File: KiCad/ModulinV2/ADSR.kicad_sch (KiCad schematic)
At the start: 71 parts, among them IC48 TL074HIDR, IC49 AS3310D, IC50 AS3310D

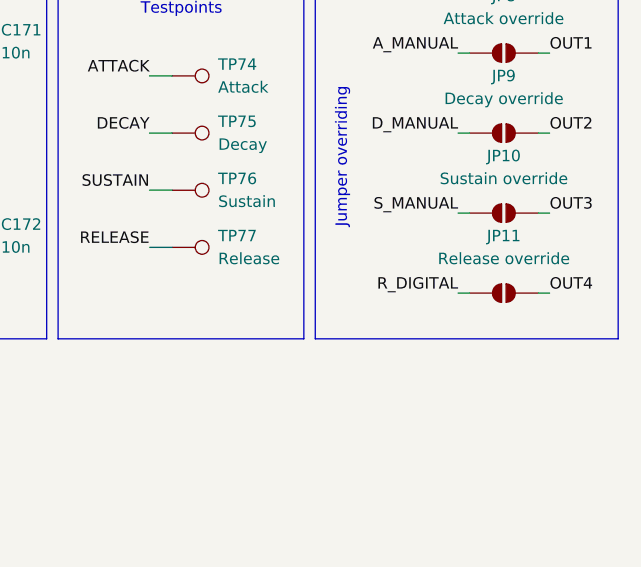
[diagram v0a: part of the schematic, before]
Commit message: Completed VCF and VCA layouts, started with ADSR
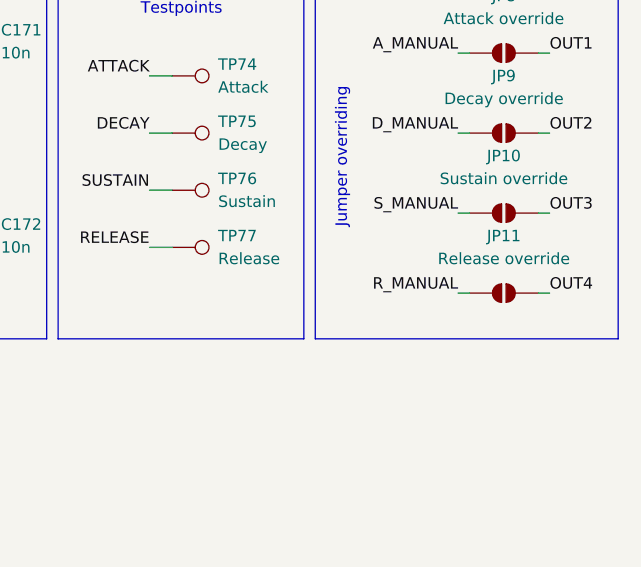
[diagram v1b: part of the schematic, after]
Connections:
- net R_DIGITAL: no longer JP11.2 (B)
- net R_MANUAL: now also JP11.2 (B)
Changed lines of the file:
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@@
 		)
 	)
-	(label "R_DIGITAL"
+	(label "R_MANUAL"
 		(at 265.43 160.02 180)
 		(effects

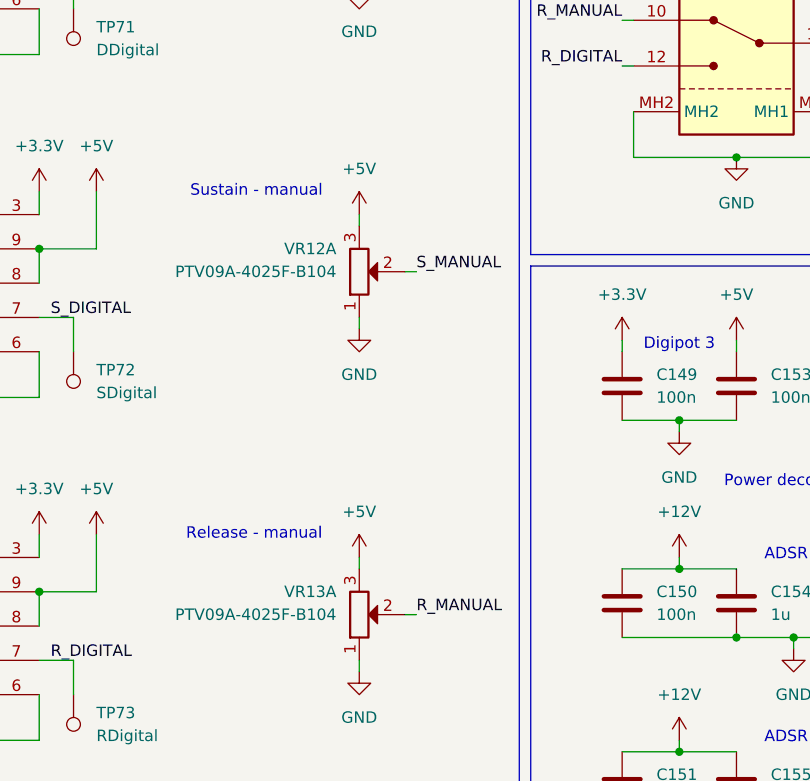
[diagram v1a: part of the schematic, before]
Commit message: Completed ADSR layout, started with Waveform select
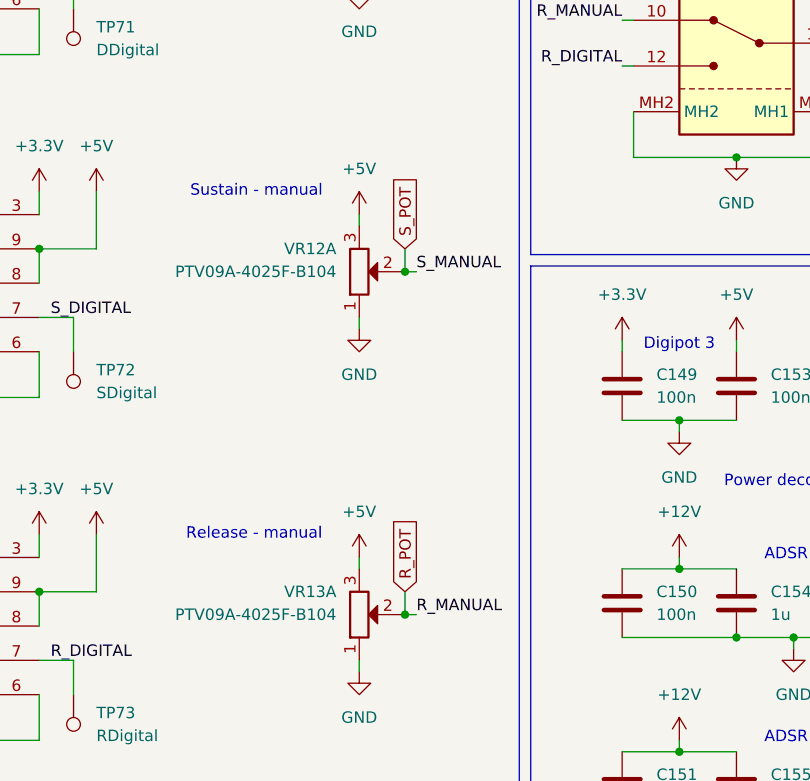
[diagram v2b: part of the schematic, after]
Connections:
- net R_MANUAL renamed R_POT
- net S_MANUAL renamed S_POT
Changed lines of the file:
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@@
 	)
 	(junction
+		(at 95.25 106.68)
+		(diameter 0)
+		(color 0 0 0 0)
+	)
+	(junction
 		(at 54.61 142.24)
 		(diameter 0)
@@
 	)
 	(junction
+		(at 95.25 144.78)
+		(diameter 0)
+		(color 0 0 0 0)
+	)
+	(junction
 		(at 171.45 87.63)
 		(diameter 0)
@@
 	(wire
 		(pts
+			(xy 95.25 142.24) (xy 95.25 144.78)
+		)
+		(stroke
+			(width 0)
+			(type default)
+		)
+	)
+	(wire
+		(pts
 			(xy 149.86 85.09) (xy 149.86 78.74)
 		)
@@
 	(wire
 		(pts
+			(xy 95.25 104.14) (xy 95.25 106.68)
+		)
+		(stroke
+			(width 0)
+			(type default)
+		)
+	)
+	(wire
+		(pts
 			(xy 171.45 55.88) (xy 166.37 55.88)
 		)
@@
 		)
 	)
+	(global_label "S_POT"
+		(shape input)
+		(at 95.25 104.14 90)
+		(fields_autoplaced yes)
+		(effects
+			(font
+				(size 1.27 1.27)
+			)
+			(justify left)
+		)
+		(property "Intersheetrefs" "${INTERSHEET_REFS}"
+			(at 95.25 95.4096 90)
+			(effects
+				(font
+					(size 1.27 1.27)
+				)
+				(justify left)
+				(hide yes)
+			)
+		)
+	)
+	(global_label "R_POT"
+		(shape input)
+		(at 95.25 142.24 90)
+		(fields_autoplaced yes)
+		(effects
+			(font
+				(size 1.27 1.27)
+			)
+			(justify left)
+		)
+		(property "Intersheetrefs" "${INTERSHEET_REFS}"
+			(at 95.25 133.4491 90)
+			(effects
+				(font
+					(size 1.27 1.27)
+				)
+				(justify left)
+				(hide yes)
+			)
+		)
+	)

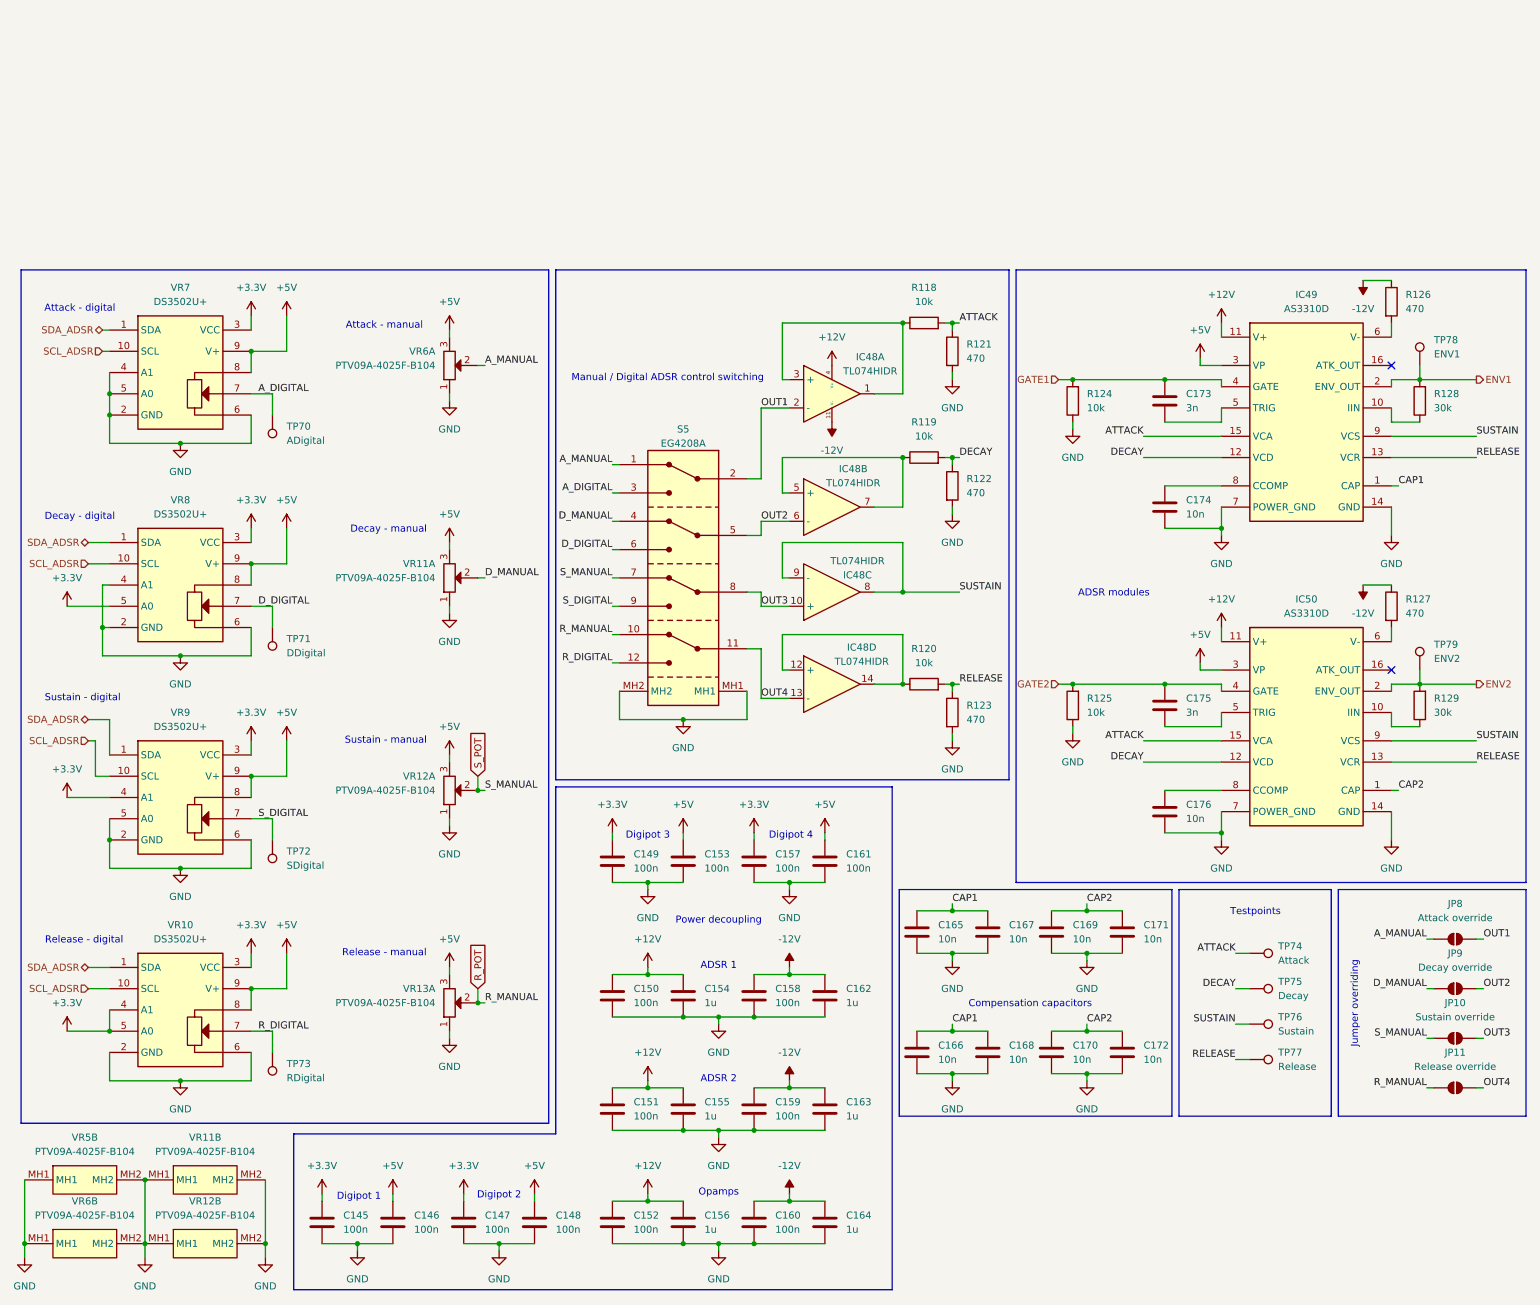
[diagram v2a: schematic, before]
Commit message: Fixed schematic connections
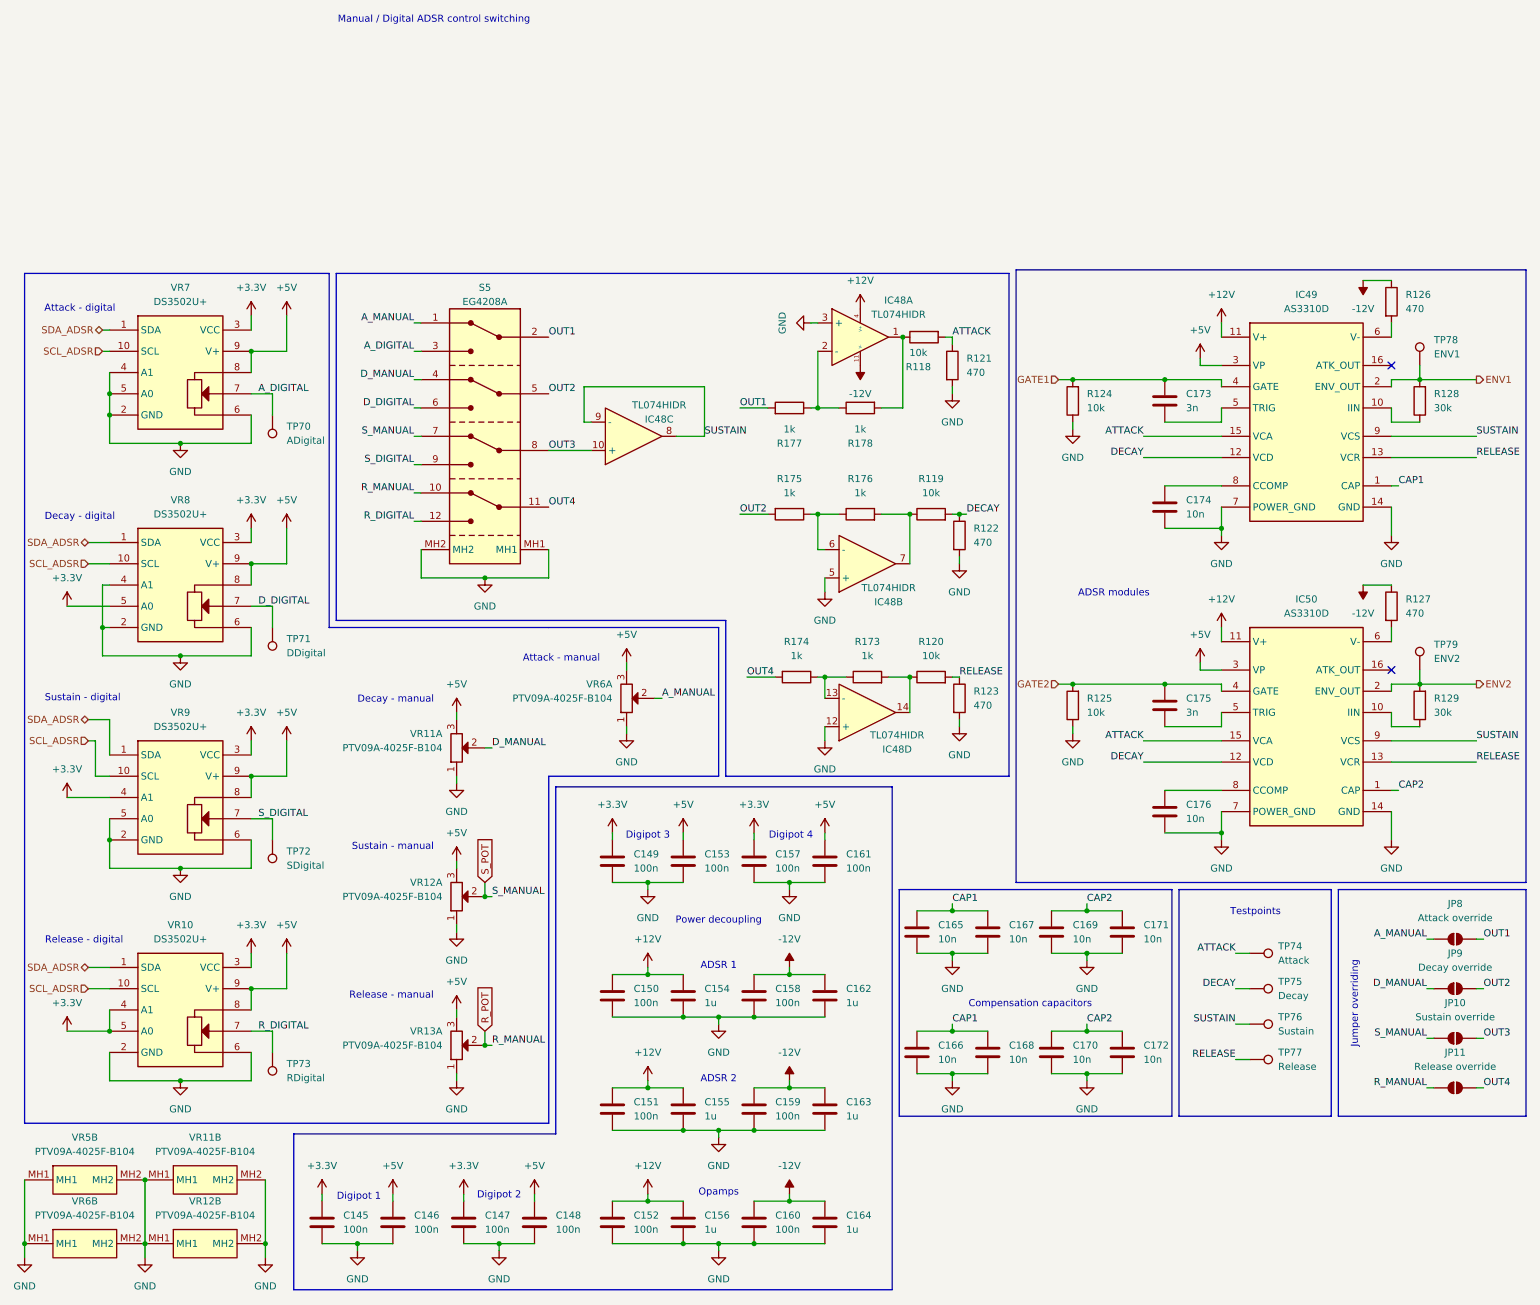
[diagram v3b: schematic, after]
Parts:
- added R173, R174, R175, R176, R177, R178: 1k, Resistor_SMD:R_0603_1608Metric_Pad0.98x0.95mm_HandSolder, symbol Device:R
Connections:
- net GND: now also IC48.12 (+), IC48.3 (+), IC48.5 (+)
- net OUT1: now also R177.2; no longer IC48.2 (-)
- net OUT2: now also R175.2; no longer IC48.6 (-)
- net OUT4: now also R174.2; no longer IC48.13 (-)
- net at IC48.1, R118.1: now also R178.2; no longer IC48.3 (+)
- net at IC48.7, R119.1: now also R176.2; no longer IC48.5 (+)
- net at IC48.14, R120.1: now also R173.2; no longer IC48.12 (+)
- new net: IC48.2 (-), R177.1, R178.1
- new net: IC48.6 (-), R175.1, R176.1
- new net: IC48.13 (-), R173.1, R174.1
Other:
- company: (none) -> TalTech
- title: (none) -> Attack Decay Sustain Release
- moved on the sheet: IC48A, IC48B, IC48C, IC48D, R118, R119, R120, R121, R122, R123, S5, VR11A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
